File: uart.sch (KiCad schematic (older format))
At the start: 5 parts, among them J2 Conn_01x06

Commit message: started pcb routing
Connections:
- net tx: now reaches J2.2 (Pin_2), R1.1
- net rx: now reaches J2.3 (Pin_3), R2.1
- net rts: now reaches J2.4 (Pin_4), R3.1
- net cts: now reaches J2.5 (Pin_5), R4.1
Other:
- moved on the sheet: J2, R1, R2, R3, R4
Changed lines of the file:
@@
 L Connector_Generic:Conn_01x06 J2
 U 1 1 5E5A7771
-P 5650 2500
-F 0 "J2" H 5730 2492 50  0000 L CNN
-F 1 "Conn_01x06" H 5730 2401 50  0000 L CNN
-F 2 "Connector_PinHeader_2.54mm:PinHeader_1x06_P2.54mm_Horizontal" H 5650 2500 50  0001 C CNN
-F 3 "~" H 5650 2500 50  0001 C CNN
-	1    5650 2500
+P 6230 3290
+F 0 "J2" H 6310 3282 50  0000 L CNN
+F 1 "Conn_01x06" H 6310 3191 50  0000 L CNN
+F 2 "Connector_PinHeader_2.54mm:PinHeader_1x06_P2.54mm_Horizontal" H 6230 3290 50  0001 C CNN
+F 3 "~" H 6230 3290 50  0001 C CNN
+	1    6230 3290
 	1    0    0    -1
 $EndComp
@@
 L power:GND #PWR0104
 U 1 1 5E5A7D94
-P 5200 3050
-F 0 "#PWR0104" H 5200 2800 50  0001 C CNN
-F 1 "GND" H 5205 2877 50  0000 C CNN
-F 2 "" H 5200 3050 50  0001 C CNN
-F 3 "" H 5200 3050 50  0001 C CNN
-	1    5200 3050
+P 5780 3840
+F 0 "#PWR0104" H 5780 3590 50  0001 C CNN
+F 1 "GND" H 5785 3667 50  0000 C CNN
+F 2 "" H 5780 3840 50  0001 C CNN
+F 3 "" H 5780 3840 50  0001 C CNN
+	1    5780 3840
 	1    0    0    -1
 $EndComp
@@
 L power:+3.3V #PWR0105
 U 1 1 5E5A8233
-P 5200 2100
-F 0 "#PWR0105" H 5200 1950 50  0001 C CNN
-F 1 "+3.3V" H 5215 2273 50  0000 C CNN
-F 2 "" H 5200 2100 50  0001 C CNN
-F 3 "" H 5200 2100 50  0001 C CNN
-	1    5200 2100
+P 5780 2890
+F 0 "#PWR0105" H 5780 2740 50  0001 C CNN
+F 1 "+3.3V" H 5795 3063 50  0000 C CNN
+F 2 "" H 5780 2890 50  0001 C CNN
+F 3 "" H 5780 2890 50  0001 C CNN
+	1    5780 2890
 	1    0    0    -1
 $EndComp
 Wire Wire Line
-	5200 2100 5200 2300
+	5780 2890 5780 3090
 Wire Wire Line
-	5200 2300 5450 2300
+	5780 3090 6030 3090
 Wire Wire Line
-	5450 2800 5200 2800
+	6030 3590 5780 3590
 Wire Wire Line
-	5200 2800 5200 3050
+	5780 3590 5780 3840
 $Comp
 L Device:R R1
 U 1 1 5E5A96F1
-P 4900 2400
-F 0 "R1" V 4850 2200 50  0000 C CNN
-F 1 "100R" V 4850 2650 50  0000 C CNN
-F 2 "Resistor_SMD:R_0805_2012Metric_Pad1.15x1.40mm_HandSolder" V 4830 2400 50  0001 C CNN
-F 3 "~" H 4900 2400 50  0001 C CNN
-	1    4900 2400
+P 5480 3190
+F 0 "R1" V 5430 2990 50  0000 C CNN
+F 1 "100R" V 5430 3440 50  0000 C CNN
+F 2 "Resistor_SMD:R_0805_2012Metric_Pad1.15x1.40mm_HandSolder" V 5410 3190 50  0001 C CNN
+F 3 "~" H 5480 3190 50  0001 C CNN
+	1    5480 3190
 	0    1    1    0
 $EndComp
@@
 L Device:R R2
 U 1 1 5E5AB560
-P 4900 2500
-F 0 "R2" V 4850 2300 50  0000 C CNN
-F 1 "100R" V 4850 2750 50  0000 C CNN
-F 2 "Resistor_SMD:R_0805_2012Metric_Pad1.15x1.40mm_HandSolder" V 4830 2500 50  0001 C CNN
-F 3 "~" H 4900 2500 50  0001 C CNN
-	1    4900 2500
+P 5480 3290
+F 0 "R2" V 5430 3090 50  0000 C CNN
+F 1 "100R" V 5430 3540 50  0000 C CNN
+F 2 "Resistor_SMD:R_0805_2012Metric_Pad1.15x1.40mm_HandSolder" V 5410 3290 50  0001 C CNN
+F 3 "~" H 5480 3290 50  0001 C CNN
+	1    5480 3290
 	0    1    1    0
 $EndComp
@@
 L Device:R R3
 U 1 1 5E5AB5F0
-P 4900 2600
-F 0 "R3" V 4850 2400 50  0000 C CNN
-F 1 "100R" V 4850 2850 50  0000 C CNN
-F 2 "Resistor_SMD:R_0805_2012Metric_Pad1.15x1.40mm_HandSolder" V 4830 2600 50  0001 C CNN
-F 3 "~" H 4900 2600 50  0001 C CNN
-	1    4900 2600
+P 5480 3390
+F 0 "R3" V 5430 3190 50  0000 C CNN
+F 1 "100R" V 5430 3640 50  0000 C CNN
+F 2 "Resistor_SMD:R_0805_2012Metric_Pad1.15x1.40mm_HandSolder" V 5410 3390 50  0001 C CNN
+F 3 "~" H 5480 3390 50  0001 C CNN
+	1    5480 3390
 	0    1    1    0
 $EndComp
@@
 L Device:R R4
 U 1 1 5E5ABA79
-P 4900 2700
-F 0 "R4" V 4850 2500 50  0000 C CNN
-F 1 "100R" V 4850 2950 50  0000 C CNN
-F 2 "Resistor_SMD:R_0805_2012Metric_Pad1.15x1.40mm_HandSolder" V 4830 2700 50  0001 C CNN
-F 3 "~" H 4900 2700 50  0001 C CNN
-	1    4900 2700
+P 5480 3490
+F 0 "R4" V 5430 3290 50  0000 C CNN
+F 1 "100R" V 5430 3740 50  0000 C CNN
+F 2 "Resistor_SMD:R_0805_2012Metric_Pad1.15x1.40mm_HandSolder" V 5410 3490 50  0001 C CNN
+F 3 "~" H 5480 3490 50  0001 C CNN
+	1    5480 3490
 	0    1    1    0
 $EndComp
 Wire Wire Line
-	5450 2500 5050 2500
+	6030 3290 5630 3290
 Wire Wire Line
-	5050 2400 5450 2400
+	5630 3190 6030 3190
 Wire Wire Line
-	5450 2600 5050 2600
+	6030 3390 5630 3390
 Wire Wire Line
-	5450 2700 5050 2700
+	6030 3490 5630 3490
 Wire Wire Line
-	4200 2400 4750 2400
+	4780 3190 5330 3190
 Wire Wire Line
-	4200 2500 4750 2500
+	4780 3290 5330 3290
 Wire Wire Line
-	4200 2600 4750 2600
+	4780 3390 5330 3390
 Wire Wire Line
-	4200 2700 4750 2700
-Text Label 4250 2400 0    50   ~ 0
+	4780 3490 5330 3490
+Text Label 4830 3190 0    50   ~ 0
 uart_tx
-Text Label 4250 2400 0    50   ~ 0
+Text Label 4830 3190 0    50   ~ 0
 uart_tx
-Text Label 4250 2500 0    50   ~ 0
+Text Label 4830 3290 0    50   ~ 0
 uart_rx
-Text Label 4250 2600 0    50   ~ 0
+Text Label 4830 3390 0    50   ~ 0
 uart_rts
-Text Label 4250 2700 0    50   ~ 0
+Text Label 4830 3490 0    50   ~ 0
 uart_cts
-Text HLabel 4200 2400 0    50   Input ~ 0
+Text HLabel 4780 3190 0    50   Input ~ 0
 uart_tx
-Text HLabel 4200 2700 0    50   Output ~ 0
+Text HLabel 4780 3490 0    50   Output ~ 0
 uart_cts
-Text HLabel 4200 2600 0    50   Input ~ 0
+Text HLabel 4780 3390 0    50   Input ~ 0
 uart_rts
-Text HLabel 4200 2500 0    50   Output ~ 0
+Text HLabel 4780 3290 0    50   Output ~ 0
 uart_rx
+Text Label 5880 3190 0    50   ~ 0
+tx
+Text Label 5880 3290 0    50   ~ 0
+rx
+Text Label 5880 3390 0    50   ~ 0
+rts
+Text Label 5880 3490 0    50   ~ 0
+cts
 $EndSCHEMATC

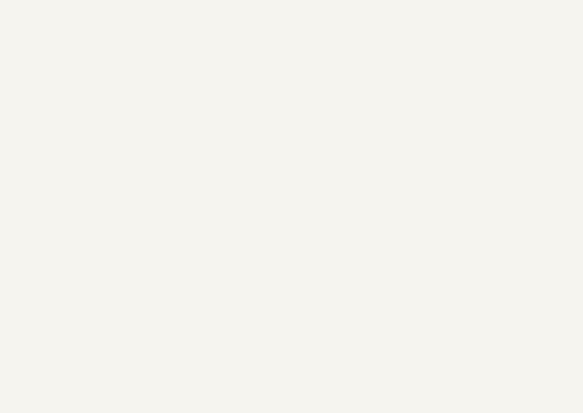
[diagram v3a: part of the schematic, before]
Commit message: layout and more silk informations
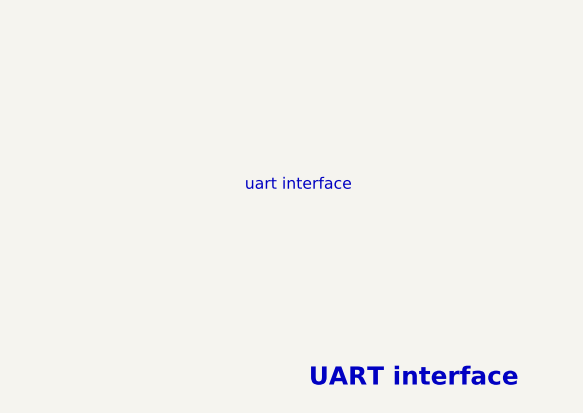
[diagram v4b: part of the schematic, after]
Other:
- note added: "UART interface"
- note added: "uart interface"
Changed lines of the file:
@@
 Text Label 5880 3490 0    50   ~ 0
 cts
+Text Notes 7330 7510 0    79   ~ 16
+UART interface
+Text Notes 7050 6650 0    50   ~ 0
+uart interface
 $EndSCHEMATC

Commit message: finished layout, created production files and added readme
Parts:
- R1, R2, R3, R4: LCSC (none) -> C17408; MPN (none) -> 0805W8F1000T5E
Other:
- note added: "1.0"
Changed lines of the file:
@@
 F 2 "Resistor_SMD:R_0805_2012Metric_Pad1.15x1.40mm_HandSolder" V 5410 3190 50  0001 C CNN
 F 3 "~" H 5480 3190 50  0001 C CNN
+F 4 "0805W8F1000T5E" H 5480 3190 50  0001 C CNN "MPN"
+F 5 "C17408" H 5480 3190 50  0001 C CNN "LCSC"
 	1    5480 3190
 	0    1    1    0
@@
 F 2 "Resistor_SMD:R_0805_2012Metric_Pad1.15x1.40mm_HandSolder" V 5410 3290 50  0001 C CNN
 F 3 "~" H 5480 3290 50  0001 C CNN
+F 4 "0805W8F1000T5E" H 5480 3290 50  0001 C CNN "MPN"
+F 5 "C17408" H 5480 3290 50  0001 C CNN "LCSC"
 	1    5480 3290
 	0    1    1    0
@@
 F 2 "Resistor_SMD:R_0805_2012Metric_Pad1.15x1.40mm_HandSolder" V 5410 3390 50  0001 C CNN
 F 3 "~" H 5480 3390 50  0001 C CNN
+F 4 "0805W8F1000T5E" H 5480 3390 50  0001 C CNN "MPN"
+F 5 "C17408" H 5480 3390 50  0001 C CNN "LCSC"
 	1    5480 3390
 	0    1    1    0
@@
 F 2 "Resistor_SMD:R_0805_2012Metric_Pad1.15x1.40mm_HandSolder" V 5410 3490 50  0001 C CNN
 F 3 "~" H 5480 3490 50  0001 C CNN
+F 4 "0805W8F1000T5E" H 5480 3490 50  0001 C CNN "MPN"
+F 5 "C17408" H 5480 3490 50  0001 C CNN "LCSC"
 	1    5480 3490
 	0    1    1    0
@@
 Text Notes 7050 6650 0    50   ~ 0
 uart interface
+Text Notes 10600 7640 0    50   ~ 0
+1.0
 $EndSCHEMATC
